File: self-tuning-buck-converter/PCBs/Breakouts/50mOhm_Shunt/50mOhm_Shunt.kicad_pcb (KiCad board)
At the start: 2 copper layers, 15.7 x 7.6 mm, 5 parts, among them J1 Input +, J2 Kelvin +, J3 Input -, J4 Kelvin -

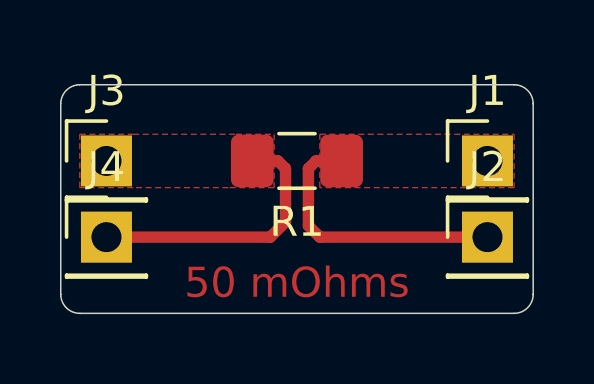
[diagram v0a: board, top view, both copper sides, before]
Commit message: began PCB design for entire buck converter
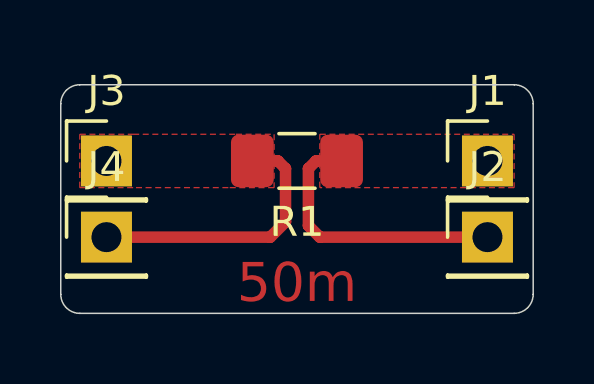
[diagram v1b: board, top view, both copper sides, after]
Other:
- board text added: "50m"
- board text removed: "50 mOhms"
